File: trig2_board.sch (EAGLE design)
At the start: 32 parts, among them IC1 SN74ACT244DW, J1 2p-2.54, J10 2p-2.54, J11 2p-2.54, J12 2p-2.54, J13 8pin, J2 2p-2.54, J3 2p-2.54, J4 2p-2.54, J5 2p-2.54, J6 2p-2.54, J7 2p-2.54, J8 2p-2.54, J9 2p-2.54, X1 BU-SMB-V, X10 BU-SMB-V, X11 BU-SMB-V, X12 BU-SMB-V, X13 87758-2816, X14 87758-2816, X15 87758-1616, X16 87758-1616, X17 87758-2816, X18 87758-2816, X2 BU-SMB-V, X3 BU-SMB-V, X4 BU-SMB-V, X5 BU-SMB-V, X6 BU-SMB-V, X7 BU-SMB-V, X8 BU-SMB-V, X9 BU-SMB-V

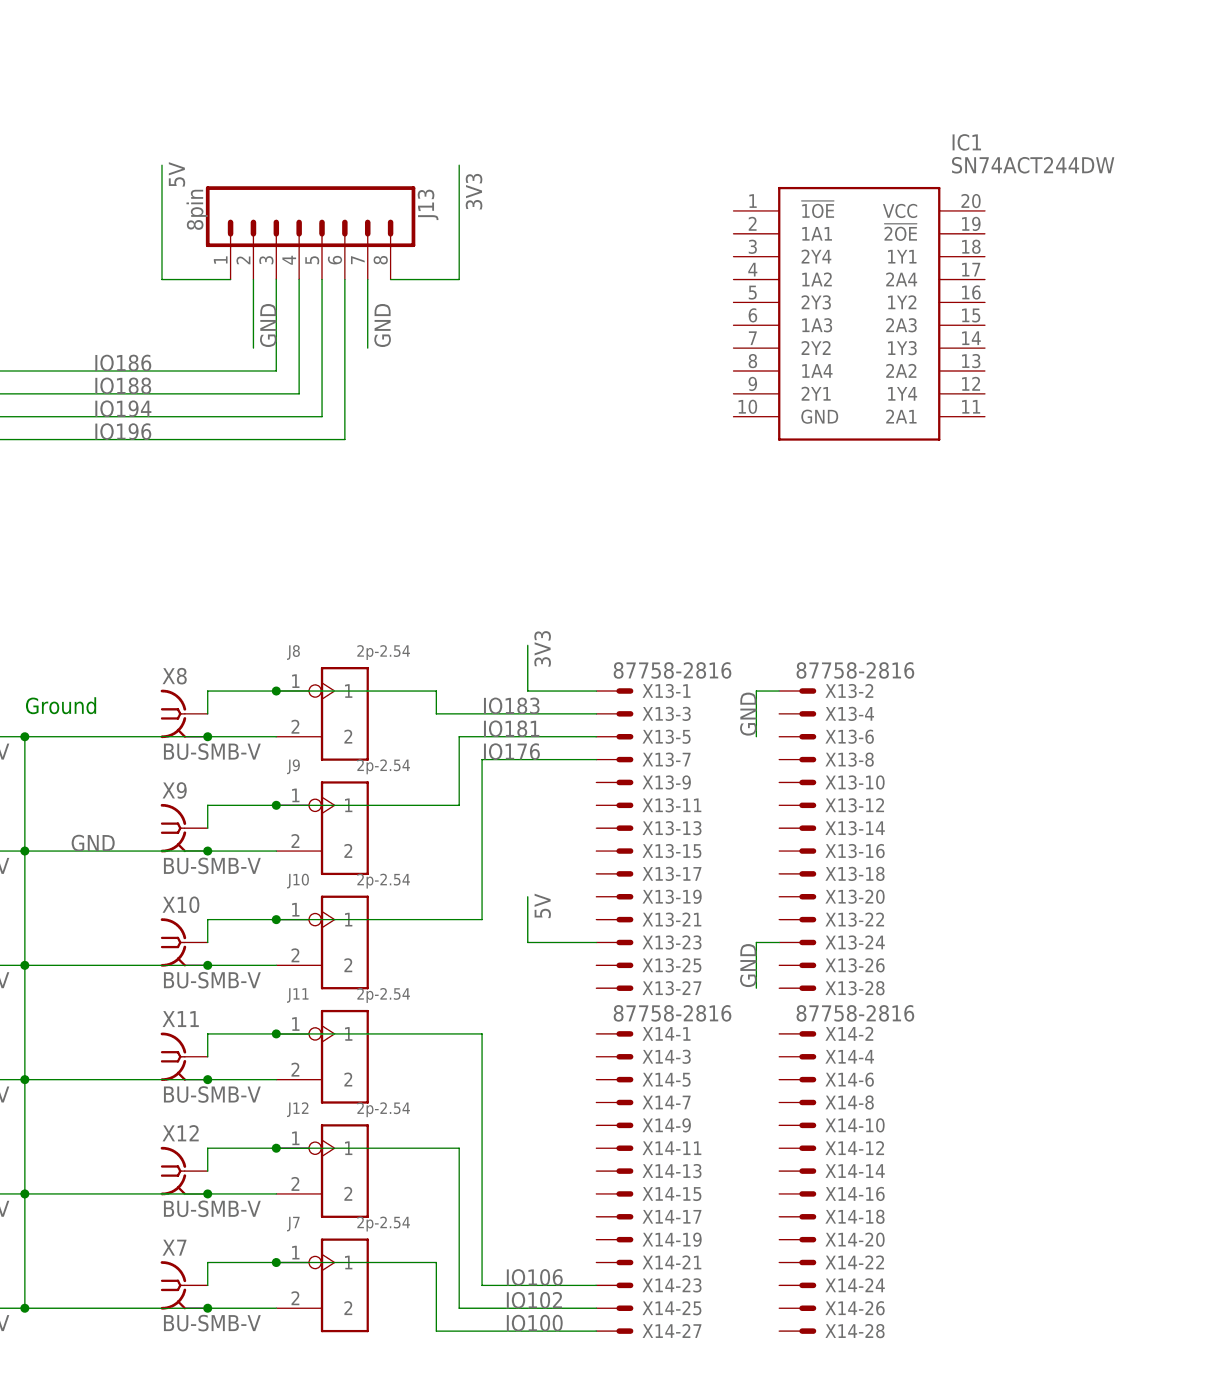
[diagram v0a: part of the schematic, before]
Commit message: autorouted with topo
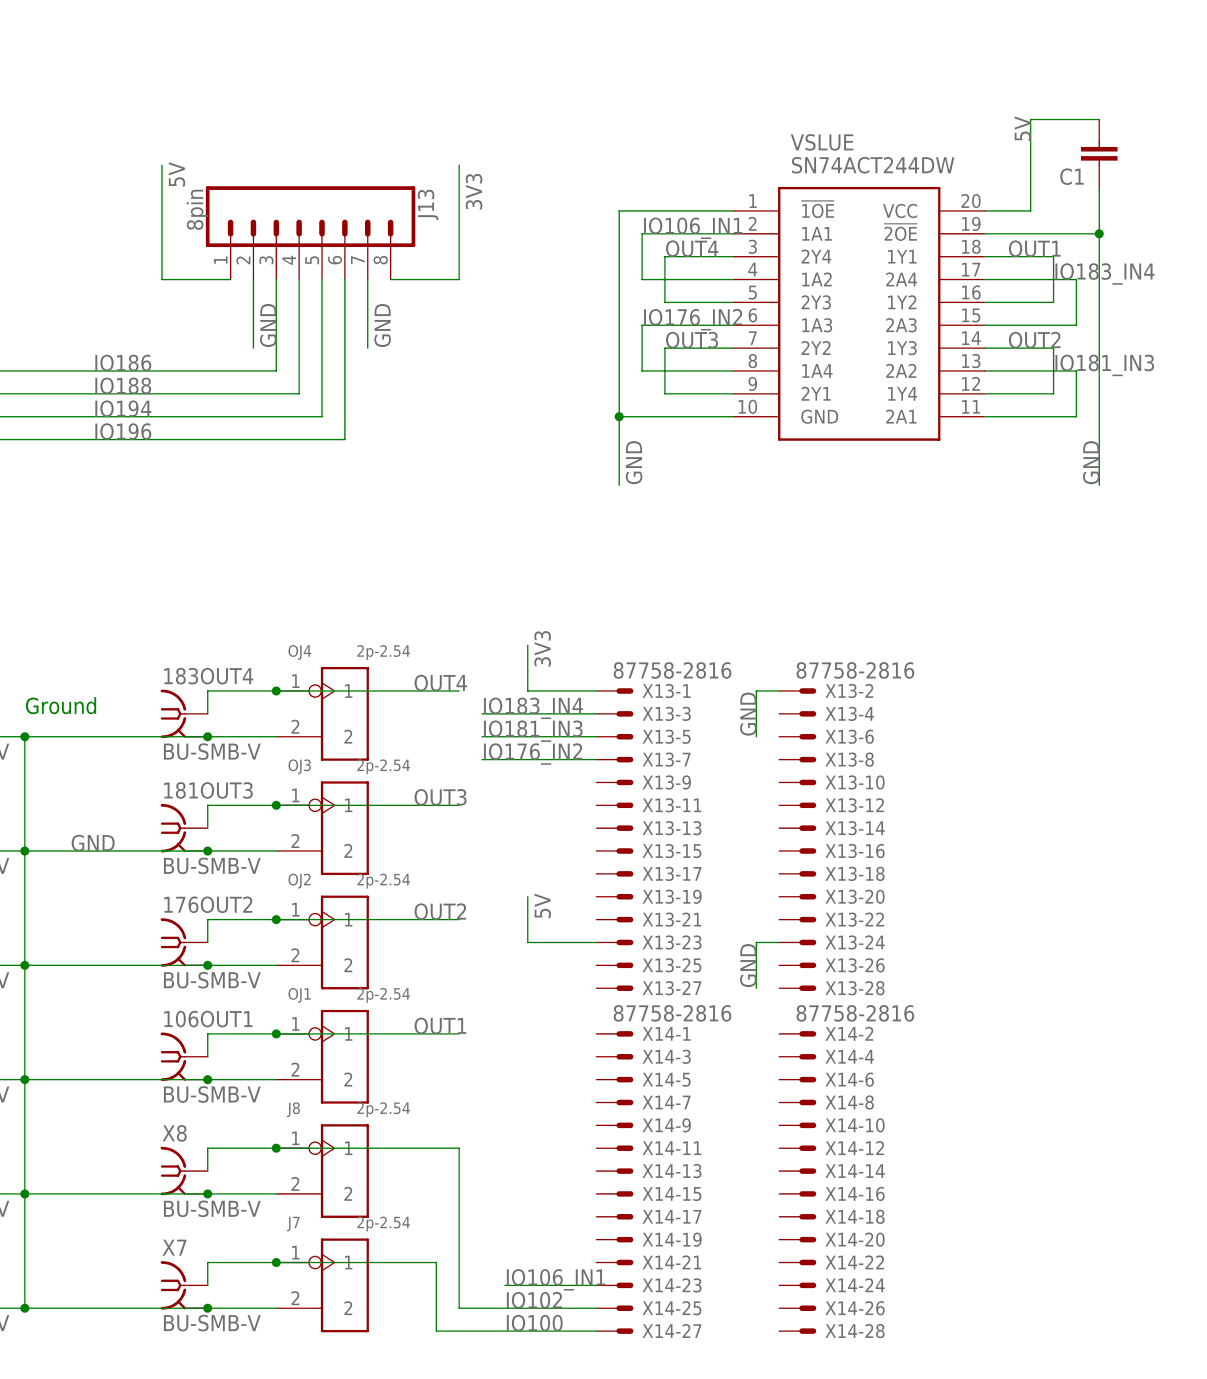
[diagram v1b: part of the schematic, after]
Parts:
- removed J12: 2p-2.54, Seeed-Connector:DIP-BLACK-MALE-HEADER-VERT(2P-2.54)
- removed X12: BU-SMB-V, con-coax:BU-SMB-V
- added 183OUT4: BU-SMB-V, con-coax:BU-SMB-V
- added C1: (no value), SparkFun-Capacitors:CAP0805
- added OJ4: 2p-2.54, Seeed-Connector:DIP-BLACK-MALE-HEADER-VERT(2P-2.54)
- renumbered IC1 to VSLUE, J10 to OJ2, J11 to OJ1, J9 to OJ3, X10 to 176OUT2, X11 to 106OUT1, X9 to 181OUT3
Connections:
- removed net IO106: 106OUT1.1, OJ1.1, X14-23.S
- removed net IO176: 176OUT2.1, OJ2.1, X13-7.S
- removed net IO181: 181OUT3.1, OJ3.1, X13-5.S
- removed net IO183: J8.1, X13-3.S, X8.1
- new net IO106_IN1: VSLUE.1A1, VSLUE.1A2, X14-23.S
- new net IO176_IN2: VSLUE.1A3, VSLUE.1A4, X13-7.S
- new net IO181_IN3: VSLUE.2A1, VSLUE.2A2, X13-5.S
- new net IO183_IN4: VSLUE.2A3, VSLUE.2A4, X13-3.S
- new net OUT1: 106OUT1.1, OJ1.1, VSLUE.1Y1, VSLUE.1Y2
- new net OUT2: 176OUT2.1, OJ2.1, VSLUE.1Y3, VSLUE.1Y4
- new net OUT3: 181OUT3.1, OJ3.1, VSLUE.2Y1, VSLUE.2Y2
- new net OUT4: 183OUT4.1, OJ4.1, VSLUE.2Y3, VSLUE.2Y4
- net 5V: now also C1.2, VSLUE.VCC
- net GND: now also 183OUT4.2, C1.1, OJ4.2, VSLUE.!1OE, VSLUE.!2OE, VSLUE.GND; no longer J12.2, X12.2
- net IO102: now also J8.1, X8.1; no longer J12.1, X12.1
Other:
- moved on the sheet: J8, X8

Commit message: with design block
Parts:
- removed 106OUT1, 176OUT2, 181OUT3, 183OUT4, X7, X8: BU-SMB-V, con-coax:BU-SMB-V
- removed J7, J8: 2p-2.54, Seeed-Connector:DIP-BLACK-MALE-HEADER-VERT(2P-2.54)
- added 174OUT, 175OUT, 176OUT, 177OUT, 181OUT, 182OUT, 183OUT, 184OUT: BU-SMB-V, con-coax:BU-SMB-V
- added C3: 0.1uF, SparkFun-Capacitors:CAP0805
- added OJ10, OJ11, OJ12, OJ9: 2p-2.54, Seeed-Connector:DIP-BLACK-MALE-HEADER-VERT(2P-2.54)
- added VSLUE2: SN74ACT244DW, SN74ACT244DW:SN74ACT244DW
- C1: value (none) -> 0.1uF
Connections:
- removed net IO100: J7.1, X14-27.S, X7.1
- removed net IO102: J8.1, X14-25.S, X8.1
- removed net IO106_IN1: VSLUE.1A1, VSLUE.1A2, X14-23.S
- new net IO174_IN1: VSLUE.1A1, VSLUE.1A2, X13-9.S
- new net IO175_IN1: VSLUE2.1A1, VSLUE2.1A2, X13-10.S
- new net IO177_IN2: VSLUE2.1A3, VSLUE2.1A4, X13-8.S
- new net IO182_IN3: VSLUE2.2A1, VSLUE2.2A2, X13-6.S
- new net IO184_IN4: VSLUE2.2A3, VSLUE2.2A4, X13-4.S
- new net OUT5: 175OUT.1, OJ12.1, VSLUE2.1Y1, VSLUE2.1Y2
- new net OUT6: 177OUT.1, OJ11.1, VSLUE2.1Y3, VSLUE2.1Y4
- new net OUT7: 182OUT.1, OJ10.1, VSLUE2.2Y1, VSLUE2.2Y2
- new net OUT8: 184OUT.1, OJ9.1, VSLUE2.2Y3, VSLUE2.2Y4
- net 3V3: no longer X18-2.S
- net 5V: now also C3.2, J13.7, VSLUE2.VCC; no longer J13.1
- net GND: now also 174OUT.2, 175OUT.2, 176OUT.2, 177OUT.2, 181OUT.2, 182OUT.2, 183OUT.2, 184OUT.2, C3.1, J13.5, J13.6, OJ10.2, OJ11.2, OJ12.2, OJ9.2, VSLUE2.!1OE, VSLUE2.!2OE, VSLUE2.GND; no longer 106OUT1.2, 176OUT2.2, 181OUT3.2, 183OUT4.2, J13.2, J13.7, J7.2, J8.2, X7.2, X8.2
- net IO186: now also J13.1; no longer J13.3
- net IO188: now also J13.2; no longer J13.4
- net IO194: now also J13.3; no longer J13.5
- net IO196: now also J13.4; no longer J13.6
- net OUT1: now also 174OUT.1; no longer 106OUT1.1
- net OUT2: now also 176OUT.1; no longer 176OUT2.1
- net OUT3: now also 181OUT.1; no longer 181OUT3.1
- net OUT4: now also 183OUT.1; no longer 183OUT4.1
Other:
- note added: "3V3"
- note removed: "Ground"
- moved on the sheet: C1, OJ1, OJ2, OJ3, OJ4, VSLUE

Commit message: 16 inputs and 16 outputs
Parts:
- removed X1, X2, X3, X4, X5, X6: BU-SMB-V, con-coax:BU-SMB-V
- added 13X6, 145OUT16, 147OUT15, 159OUT14, 161OUT13, 164OUT12, 167OUT11, 169OUT10, 173OUT9, 19X7, 21X8, 236X1, 238X2, 240X3, 37X9, 39X10, 43X11, 45X12, 49X13, 4X4, 51X14, 55X15, 57X16, 6X5: BU-SMB-V, con-coax:BU-SMB-V
- added C2, C4: 0.1uF, SparkFun-Capacitors:CAP0805
- added J10, J11, J12, J14, J15, J16, J17, J7, J8, J9, OJ13, OJ14, OJ15, OJ16, OJ17, OJ18, OJ19, OJ20: 2p-2.54, Seeed-Connector:DIP-BLACK-MALE-HEADER-VERT(2P-2.54)
- added J18: 8pin, SparkFun-Connectors:CONN_08"
- added R1, R10, R11, R12, R13, R14, R15, R16, R2, R3, R4, R5, R6, R7, R8, R9: 50, SparkFun-Passives:RESISTORAXIAL-0.3
- added VSLUE3, VSLUE4: SN74ACT244DW, SN74ACT244DW:SN74ACT244DW
- renumbered 174OUT to 174OUT1, 175OUT to 175OUT5, 176OUT to 176OUT2, 177OUT to 177OUT6, 181OUT to 181OUT3, 182OUT to 182OUT7, 183OUT to 183OUT4, 184OUT to 184OUT8
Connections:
- removed net IO186: J13.1, X15-15.S
- removed net IO188: J13.2, X15-13.S
- removed net IO194: J13.3, X15-11.S
- removed net IO196: J13.4, X15-9.S
- removed net IO85: J4.2, X17-24.S, X4.1
- removed net IO87: J5.2, X17-26.S, X5.1
- removed net IO94: J6.2, X17-28.S, X6.1
- new net IO13: 13X6.1, J9.2, R9.2, X18-14.S
- new net IO145_IN4: VSLUE4.2A3, VSLUE4.2A4, X13-28.S
- new net IO147_IN3: VSLUE4.2A1, VSLUE4.2A2, X13-26.S
- new net IO159_IN2: VSLUE4.1A3, VSLUE4.1A4, X13-22.S
- new net IO161_IN1: VSLUE4.1A1, VSLUE4.1A2, X13-20.S
- new net IO164_IN4: VSLUE3.2A3, VSLUE3.2A4, X13-18.S
- new net IO167_IN3: VSLUE3.2A1, VSLUE3.2A2, X13-16.S
- new net IO169_IN2: VSLUE3.1A3, VSLUE3.1A4, X13-14.S
- new net IO173_IN1: VSLUE3.1A1, VSLUE3.1A2, X13-12.S
- new net IO185: J18.8, X15-16.S
- new net IO187: J18.7, X15-14.S
- new net IO189: J18.6, X15-12.S
- new net IO19: 19X7.1, J10.2, R10.2, X18-16.S
- new net IO195: J18.5, X15-10.S
- new net IO197: J18.4, X15-8.S
- new net IO199: J18.3, X15-6.S
- new net IO201: J18.2, X15-4.S
- new net IO203: J18.1, X15-2.S
- new net IO21: 21X8.1, J11.2, R11.2, X18-18.S
- new net IO37: 37X9.1, J12.2, R12.2, X18-20.S
- new net IO39: 39X10.1, J14.2, R13.2, X18-22.S
- new net IO4: 4X4.1, J7.2, R7.2, X18-10.S
- new net IO43: 43X11.1, J15.2, R14.2, X18-26.S
- new net IO45: 45X12.1, J16.2, R15.2, X18-28.S
- new net IO49: 49X13.1, J17.2, R16.2, X17-2.S
- new net IO51: 51X14.1, J4.2, R4.2, X17-4.S
- new net IO55: 55X15.1, J5.2, R5.2, X17-6.S
- new net IO57: 57X16.1, J6.2, R6.2, X17-8.S
- new net IO6: 6X5.1, J8.2, R8.2, X18-12.S
- new net OUT10: 169OUT10.1, OJ15.1, VSLUE3.1Y3, VSLUE3.1Y4
- new net OUT11: 167OUT11.1, OJ14.1, VSLUE3.2Y1, VSLUE3.2Y2
- new net OUT12: 164OUT12.1, OJ13.1, VSLUE3.2Y3, VSLUE3.2Y4
- new net OUT13: 161OUT13.1, OJ20.1, VSLUE4.1Y1, VSLUE4.1Y2
- new net OUT14: 159OUT14.1, OJ19.1, VSLUE4.1Y3, VSLUE4.1Y4
- new net OUT15: 147OUT15.1, OJ18.1, VSLUE4.2Y1, VSLUE4.2Y2
- new net OUT16: 145OUT16.1, OJ17.1, VSLUE4.2Y3, VSLUE4.2Y4
- new net OUT9: 173OUT9.1, OJ16.1, VSLUE3.1Y1, VSLUE3.1Y2
- net 3V3: now also J13.7; no longer J13.8
- net 5V: now also C2.2, C4.2, J13.5, VSLUE3.VCC, VSLUE4.VCC; no longer J13.7
- net GND: now also 13X6.2, 145OUT16.2, 147OUT15.2, 159OUT14.2, 161OUT13.2, 164OUT12.2, 167OUT11.2, 169OUT10.2, 173OUT9.2, 19X7.2, 21X8.2, 236X1.2, 238X2.2, 240X3.2, 37X9.2, 39X10.2, 43X11.2, 45X12.2, 49X13.2, 4X4.2, 51X14.2, 55X15.2, 57X16.2, 6X5.2, C2.1, C4.1, J10.1, J11.1, J12.1, J13.8, J14.1, J15.1, J16.1, J17.1, J7.1, J8.1, J9.1, OJ13.2, OJ14.2, OJ15.2, OJ16.2, OJ17.2, OJ18.2, OJ19.2, OJ20.2, R1.1, R10.1, R11.1, R12.1, R13.1, R14.1, R15.1, R16.1, R2.1, R3.1, R4.1, R5.1, R6.1, R7.1, R8.1, R9.1, VSLUE3.!1OE, VSLUE3.!2OE, VSLUE3.GND, VSLUE4.!1OE, VSLUE4.!2OE, VSLUE4.GND; no longer J13.5, X1.2, X2.2, X3.2, X4.2, X5.2, X6.2
- net IO236: now also 236X1.1, R1.2; no longer X1.1
- net IO238: now also 238X2.1, R2.2; no longer X2.1
- net IO240: now also 240X3.1, R3.2; no longer X3.1
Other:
- moved on the sheet: C3, J13, J4, J5, J6, X17-1, X17-10, X17-11, X17-12, X17-13, X17-14, X17-15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
